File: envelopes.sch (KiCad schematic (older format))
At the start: 96 parts

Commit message: ENV1 inverter circuitry captured and simulated.
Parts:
- removed R? (x4): 100K, MyModules:SM0603-R-JRL, symbol R_US
- removed R? (x4): 10K, MyModules:SM0603-R-JRL, symbol R_US
- removed TP? (x4): TEST_POINT, MyModules:TEST_POINT_5000_SERIES, symbol TEST_POINT
- removed U?: TL074-, Housings_SSOP:TSSOP-14_4.4x5mm_Pitch0.65mm, symbol TL074-
- added Q?: MMBT3904, SOT-23, symbol MMBT3904
- added R? (x3): 100K, MyModules:SM0603-R-JRL, symbol R_US
- added R?: 10K, MyModules:SM0603-R-JRL, symbol R_US
- added R?: 47K, MyModules:SM0603-R-JRL, symbol R_US
- added U?: TL074-, Housings_SSOP:TSSOP-14_4.4x5mm_Pitch0.65mm, symbol TL074-
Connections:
- net EG2_GATE is gone; now on net GATE: R?.1, R?.2
- net GND: now also Q?.2 (E)
- net EG1_ATTACK_CV renamed ENV1_A
- net EG1_DECAY_CV renamed ENV1_D
- net EG1_ENV_OUT: no longer names the net of C?.1, R?.2, U?.1, U?.6 (THR)
- net EG1_ENV_OUT: now also R?.1, R?.1
- net EG1_GATE renamed GATE
- removed net EG1_INV_OUT: U?.1
- net EG1_RELEASE_CV renamed ENV1_R
- net EG1_SUSTAIN_CV renamed ENV1_S
- net EG2_ATTACK_CV renamed ENV2_A
- net EG2_DECAY_CV renamed ENV2_D
- net EG2_ENV_OUT: no longer names the net of C?.1, R?.2, U?.1, U?.6 (THR)
- net EG2_ENV_OUT: now also U?.12 (+)
- net EG2_RELEASE_CV renamed ENV2_R
- net EG2_SUSTAIN_CV renamed ENV2_S
- new net: R?.2, U?.12 (+)
- new net: R?.1, R?.2, U?.13 (-)
- new net: Q?.1 (B), R?.1
- new net: Q?.3 (C), R?.1, R?.2
- new net ENV1_POL: R?.2
- new net ENV_1: R?.2, U?.14
- new net ENV_2: U?.13 (-), U?.14
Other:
- note added: "ENV1 inversion works\nin simulation"
- moved on the sheet: C?, Q?, Q?A, R?, TP?, U?, U?A

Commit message: put oscillators into subsheet. slogging through ENV1/ENV2 switching
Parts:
- removed TP? (x4): TEST_POINT, MyModules:TEST_POINT_5000_SERIES, symbol TEST_POINT
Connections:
- net GND: now also U?.5 (+); no longer U?.3 (+)
- net at C?.1, R?.2, U?.12 (+)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: now also U?.7; no longer U?.1
- net at R?.1, R?.2, TP?.1: now also U?.8; no longer U?.1
- net at R?.1, R?.2: now also U?.9 (-); no longer U?.2 (-)
- net at R?.1, R?.2: now also U?.10 (+); no longer U?.3 (+)
- net at C?.2, Q?.6, Q?.6: now also U?.6 (-); no longer U?.2 (-)
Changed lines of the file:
@@
 $Descr D 34000 22000
 encoding utf-8
-Sheet 2 2
+Sheet 2 3
 Title ""
 Date ""
@@
 P 4075 9975
 F 0 "#PWR?" H 4075 10075 30  0001 C CNN
-F 1 "+12V" H 4050 10250 60  0000 C CNN
+F 1 "+12V" H 4050 10150 60  0000 C CNN
 F 2 "~" H 4075 9975 60  0000 C CNN
 F 3 "~" H 4075 9975 60  0000 C CNN
@@
 $Comp
 L TL074- U?
-U 1 1 57F64195
+U 3 1 57F64195
 P 25200 13700
 F 0 "U?" H 25250 13900 60  0000 C CNN
@@
 F 2 "Housings_SSOP:TSSOP-14_4.4x5mm_Pitch0.65mm" H 25200 13700 60  0001 C CNN
 F 3 "" H 25200 13700 60  0000 C CNN
-	1    25200 13700
+	3    25200 13700
 	-1   0    0    -1
 $EndComp
@@
 $Comp
 L TL074- U?
-U 1 1 57F641D3
+U 2 1 57F641D3
 P 26100 11125
 F 0 "U?" H 26150 11325 60  0000 C CNN
@@
 F 2 "Housings_SSOP:TSSOP-14_4.4x5mm_Pitch0.65mm" H 26100 11125 60  0001 C CNN
 F 3 "" H 26100 11125 60  0000 C CNN
-	1    26100 11125
+	2    26100 11125
 	1    0    0    -1
 $EndComp
@@
 P 19200 9975
 F 0 "#PWR?" H 19200 10075 30  0001 C CNN
-F 1 "+12V" H 19175 10250 60  0000 C CNN
+F 1 "+12V" H 19175 10150 60  0000 C CNN
 F 2 "~" H 19200 9975 60  0000 C CNN
 F 3 "~" H 19200 9975 60  0000 C CNN
@@
 $EndComp
 $Comp
-L TEST_POINT TP?
-U 1 1 57F64304
-P 21000 10725
-F 0 "TP?" V 21150 10675 60  0000 L CNN
-F 1 "TEST_POINT" H 21000 10780 30  0001 C CNN
-F 2 "MyModules:TEST_POINT_5000_SERIES" H 21000 10725 60  0001 C CNN
-F 3 "" H 21000 10725 60  0000 C CNN
-	1    21000 10725
-	0    -1   -1   0
-$EndComp
-$Comp
-L TEST_POINT TP?
-U 1 1 57F6430B
-P 20475 10725
-F 0 "TP?" V 20625 10675 60  0000 L CNN
-F 1 "TEST_POINT" H 20475 10780 30  0001 C CNN
-F 2 "MyModules:TEST_POINT_5000_SERIES" H 20475 10725 60  0001 C CNN
-F 3 "" H 20475 10725 60  0000 C CNN
-	1    20475 10725
-	0    -1   -1   0
-$EndComp
-$Comp
 L R_US R?
 U 1 1 57F64312
@@
 F 3 "" H 20700 10975 60  0000 C CNN
 	1    20700 10975
-	0    -1   -1   0
-$EndComp
-$Comp
-L TEST_POINT TP?
-U 1 1 57F64319
-P 20925 12125
-F 0 "TP?" V 20925 11900 60  0000 L CNN
-F 1 "TEST_POINT" H 20925 12180 30  0001 C CNN
-F 2 "MyModules:TEST_POINT_5000_SERIES" H 20925 12125 60  0001 C CNN
-F 3 "" H 20925 12125 60  0000 C CNN
-	1    20925 12125
-	0    -1   -1   0
-$EndComp
-$Comp
-L TEST_POINT TP?
-U 1 1 57F64320
-P 20400 12125
-F 0 "TP?" V 20400 12225 60  0000 L CNN
-F 1 "TEST_POINT" H 20400 12180 30  0001 C CNN
-F 2 "MyModules:TEST_POINT_5000_SERIES" H 20400 12125 60  0001 C CNN
-F 3 "" H 20400 12125 60  0000 C CNN
-	1    20400 12125
 	0    -1   -1   0
 $EndComp
@@
 	20900 10975 22650 10975
 Wire Wire Line
-	21000 10875 21000 10975
-Connection ~ 21000 10975
-Wire Wire Line
 	20250 12375 20450 12375
 Connection ~ 22300 10975
@@
 Connection ~ 24700 9575
 Wire Wire Line
-	20475 10875 20475 10975
-Connection ~ 20475 10975
-Wire Wire Line
 	21050 12375 21050 12675
-Wire Wire Line
-	20925 12275 20925 12375
-Wire Wire Line
-	20400 12275 20400 12375
-Connection ~ 20925 12375
-Connection ~ 20400 12375
 Connection ~ 24325 13700
 Wire Wire Line
@@
 U 1 1 57F684B3
 P 3475 9525
-F 0 "Q?" H 3675 9600 50  0000 L CNN
-F 1 "MMBT3904" H 3675 9525 50  0000 L CNN
-F 2 "SOT-23" H 3675 9450 50  0000 L CIN
+F 0 "Q?" H 3375 9825 50  0000 L CNN
+F 1 "MMBT3904" H 3100 9750 50  0000 L CNN
+F 2 "SOT-23" H 3675 9450 50  0001 L CIN
 F 3 "" H 3475 9525 50  0000 L CNN
 	1    3475 9525
@@
 U 1 1 57F68A9B
 P 18600 9525
-F 0 "Q?" H 18800 9600 50  0000 L CNN
-F 1 "MMBT3904" H 18800 9525 50  0000 L CNN
-F 2 "SOT-23" H 18800 9450 50  0000 L CIN
+F 0 "Q?" H 18500 9850 50  0000 L CNN
+F 1 "MMBT3904" H 18275 9750 50  0000 L CNN
+F 2 "SOT-23" H 18800 9450 50  0001 L CIN
 F 3 "" H 18600 9525 50  0000 L CNN
 	1    18600 9525

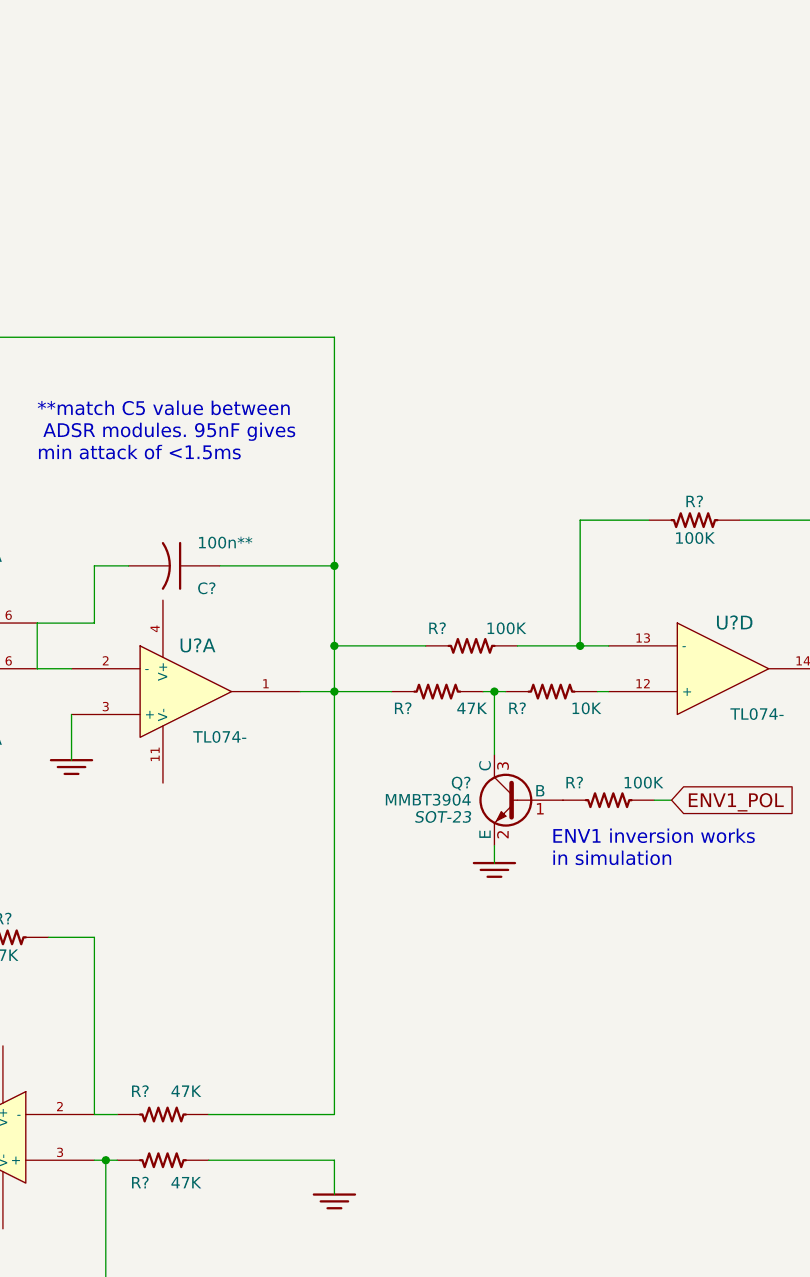
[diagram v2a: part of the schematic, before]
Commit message: working on a cross talk reduction circuit for CD4053. Seems pointless as it only works with unipolar signals. Try again another day stupid
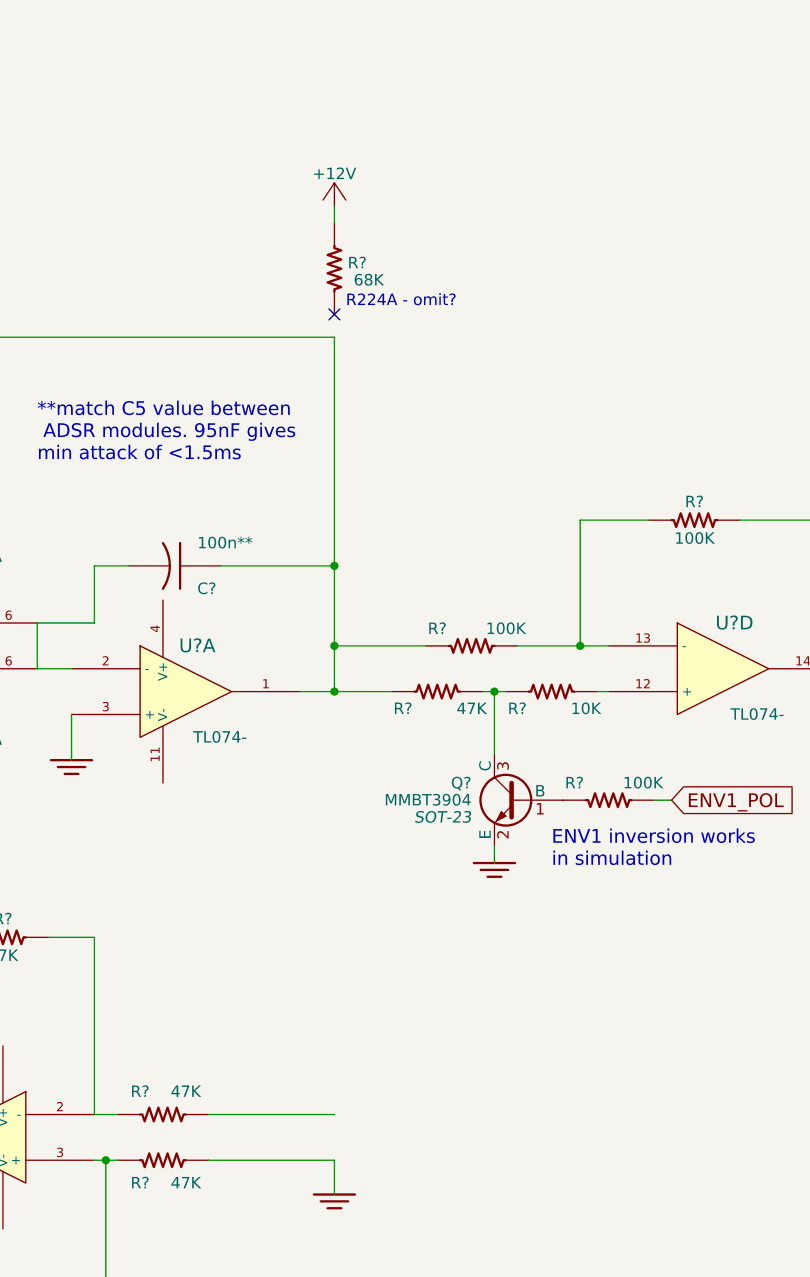
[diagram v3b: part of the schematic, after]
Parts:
- added R?: 68K, MyModules:SM0603-R-JRL, symbol R_US
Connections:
- net +12V: now also R?.2
- net at C?.1, R?.1, R?.1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: no longer R?.2
- no-connect marks 2 -> 3
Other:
- note added: "R224A - omit?"
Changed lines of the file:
@@
 	6325 9575 11625 9575
-Wire Wire Line
-	11625 9575 11625 12975
 Wire Wire Line
 	5925 12375 5925 12675
@@
 Text Notes 12575 11900 0    60   ~ 0
 ENV1 inversion works\nin simulation
+$Comp
+L R_US R?
+U 1 1 57FCB1DF
+P 11625 9275
+F 0 "R?" H 11525 9250 50  0000 C CNN
+F 1 "68K" H 11475 9325 50  0000 C CNN
+F 2 "MyModules:SM0603-R-JRL" H 11625 9275 60  0001 C CNN
+F 3 "" H 11625 9275 60  0001 C CNN
+F 4 "P10.0KCCT-ND" V 11625 9275 60  0001 C CNN "Digikey"
+	1    11625 9275
+	-1   0    0    1
+$EndComp
+$Comp
+L +12V #PWR?
+U 1 1 57FCB1E6
+P 11625 9000
+F 0 "#PWR?" H 11625 8850 50  0001 C CNN
+F 1 "+12V" H 11625 9140 50  0000 C CNN
+F 2 "" H 11625 9000 60  0000 C CNN
+F 3 "" H 11625 9000 60  0000 C CNN
+	1    11625 9000
+	-1   0    0    -1
+$EndComp
+Wire Wire Line
+	11625 9000 11625 9075
+Wire Wire Line
+	11625 9575 11625 11125
+NoConn ~ 11625 9475
+Text Notes 11675 9450 0    50   ~ 0
+R224A - omit?
 $EndSCHEMATC

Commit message: module board schematic basically captured. Need to doublecheck and confirm and try to simulation of VCA and VCF control
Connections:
- net at R?.2: now also C?.1, R?.1, R?.1, U?.1, U?.6 (THR)
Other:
- note added: "ENV 1"
- note added: "ENV 2"
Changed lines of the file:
@@
 Connection ~ 9425 10825
-Wire Wire Line
-	10325 10825 10325 11025
 Wire Wire Line
 	8525 10825 8525 11025
@@
 Connection ~ 24550 10825
 Wire Wire Line
-	25450 10825 25450 11025
-Wire Wire Line
 	23650 10825 23650 11025
 Wire Wire Line
@@
 F 0 "Q?" H 12625 11675 50  0000 L CNN
 F 1 "MMBT3904" H 12625 11600 50  0000 L CNN
-F 2 "SOT-23" H 12625 11525 50  0000 L CIN
+F 2 "SOT-23" H 12625 11525 50  0001 L CIN
 F 3 "" H 12425 11600 50  0000 L CNN
 	1    12425 11600
@@
 	11625 9000 11625 9075
 Wire Wire Line
-	11625 9575 11625 11125
+	11625 9575 11625 12975
 NoConn ~ 11625 9475
 Text Notes 11675 9450 0    50   ~ 0
 R224A - omit?
+Text Notes 3575 8350 0    200  ~ 40
+ENV 1
+Text Notes 18650 8350 0    200  ~ 40
+ENV 2
+Wire Wire Line
+	10400 10825 10400 11025
+Connection ~ 10400 11025
+Connection ~ 10400 10825
+Wire Wire Line
+	25525 10825 25525 11025
+Connection ~ 25525 11025
+Connection ~ 25525 10825
 $EndSCHEMATC

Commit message: sorting out packages, also taking deeper look at saw to tri converter. there are problems on 12V power and 10V saw that need to be sorted. NPN in tri converter is a an ultra fast switcher that might be hard to find an equiavalent for. Worth looking at tri waveform out of converter on JP8
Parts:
- gave numbers to parts that had none: 6
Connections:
- net ENV_1: now also U25.8; no longer U25.14
- net GND: now also U25.5 (+); no longer U25.3 (+)
- net at R?.2: now also U25.10 (+); no longer U25.12 (+)
- net at R?.1, R?.2: now also U25.9 (-); no longer U25.13 (-)
- net at R?.1, R?.2, TP?.1: now also U25.14; no longer U25.1
- net at R?.1, R?.2: now also U25.13 (-); no longer U25.2 (-)
- net at R?.1, R?.2: now also U25.12 (+); no longer U25.3 (+)
- net at C?.1, R?.1, R?.1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: now also U25.7; no longer U25.1
- net at C?.2, Q?.6, Q?.6: now also U25.6 (-); no longer U25.2 (-)
- net at R?.1, R?.2: now also U28.5 (+); no longer U28.10 (+)
- net at R?.1, R?.2, TP?.1: now also U28.7; no longer U28.8
- net at R?.1, R?.2: now also U28.6 (-); no longer U28.9 (-)

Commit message: more transistor swapping
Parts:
- removed Q? (x3): MMBT3904, SOT-23, symbol MMBT3904
- removed TP? (x4): TEST_POINT, MyModules:TEST_POINT_5000_SERIES, symbol TEST_POINT
- added Q? (x3): 2SC4738, SOT-23, symbol 2SC4738
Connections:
- net GND: now also Q?.2 (E), Q?.2 (E), Q?.2 (E)
- net at R?.1: now also Q?.1 (B)
- net at R?.1, R?.2: now also Q?.3 (C)
- net at C?.1, R?.1, U26.10 (A): now also Q?.3 (C)
- net at R?.1, R?.1: now also Q?.1 (B) (x2)
- net at C?.1, R?.1, U29.10 (A): now also Q?.3 (C)
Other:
- note added: "Change to PMP4201/5201 pairs?"
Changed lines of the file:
@@
-	0    -1   -1   0
-$EndComp
-$Comp
-L TEST_POINT TP?
-U 1 1 57F5ECCA
-P 9200 13525
-F 0 "TP?" V 9350 13475 60  0000 L CNN
-F 1 "TEST_POINT" H 9200 13580 30  0001 C CNN
-F 2 "MyModules:TEST_POINT_5000_SERIES" H 9200 13525 60  0001 C CNN
-F 3 "" H 9200 13525 60  0000 C CNN
-	1    9200 13525
-	0    -1   -1   0
-$EndComp
-$Comp
-L TEST_POINT TP?
-U 1 1 57F5ECD1
-P 8675 13525
-F 0 "TP?" V 8825 13475 60  0000 L CNN
-F 1 "TEST_POINT" H 8675 13580 30  0001 C CNN
-F 2 "MyModules:TEST_POINT_5000_SERIES" H 8675 13525 60  0001 C CNN
-F 3 "" H 8675 13525 60  0000 C CNN
-	1    8675 13525
 	0    -1   -1   0
 $EndComp
@@
 Wire Wire Line
 	5925 12375 5925 12675
-Connection ~ 9200 13675
 Wire Wire Line
 	4075 9975 4075 10150
 Wire Wire Line
 	4075 10150 4425 10150
-Connection ~ 8675 13675
 Connection ~ 9575 13075
 $Comp
@@
 $EndComp
 $Comp
-L TEST_POINT TP?
-U 1 1 57F6432E
-P 24325 13550
-F 0 "TP?" V 24475 13500 60  0000 L CNN
-F 1 "TEST_POINT" H 24325 13605 30  0001 C CNN
-F 2 "MyModules:TEST_POINT_5000_SERIES" H 24325 13550 60  0001 C CNN
-F 3 "" H 24325 13550 60  0000 C CNN
-	1    24325 13550
-	0    -1   -1   0
-$EndComp
-$Comp
-L TEST_POINT TP?
-U 1 1 57F64335
-P 23800 13550
-F 0 "TP?" V 23950 13500 60  0000 L CNN
-F 1 "TEST_POINT" H 23800 13605 30  0001 C CNN
-F 2 "MyModules:TEST_POINT_5000_SERIES" H 23800 13550 60  0001 C CNN
-F 3 "" H 23800 13550 60  0000 C CNN
-	1    23800 13550
-	0    -1   -1   0
-$EndComp
-$Comp
 L DMMT3906 Q?
 U 1 1 57F6433C
@@
 Wire Wire Line
 	26750 9575 26750 13600
-Connection ~ 24700 9575
 Wire Wire Line
 	21050 12375 21050 12675
-Connection ~ 24325 13700
 Wire Wire Line
 	19200 9975 19200 10150
 Wire Wire Line
 	19200 10150 19550 10150
-Connection ~ 23800 13700
-$Comp
-L MMBT3904 Q?
-U 1 1 57F684B3
-P 3475 9525
-F 0 "Q?" H 3375 9825 50  0000 L CNN
-F 1 "MMBT3904" H 3100 9750 50  0000 L CNN
-F 2 "SOT-23" H 3675 9450 50  0001 L CIN
-F 3 "" H 3475 9525 50  0000 L CNN
-	1    3475 9525
-	1    0    0    -1
-$EndComp
-$Comp
-L MMBT3904 Q?
-U 1 1 57F68A9B
-P 18600 9525
-F 0 "Q?" H 18500 9850 50  0000 L CNN
-F 1 "MMBT3904" H 18275 9750 50  0000 L CNN
-F 2 "SOT-23" H 18800 9450 50  0001 L CIN
-F 3 "" H 18600 9525 50  0000 L CNN
-	1    18600 9525
-	1    0    0    -1
-$EndComp
 Wire Wire Line
 	27400 10925 27400 10300
@@
 	13825 11025 14025 11025
 Connection ~ 13900 11025
-$Comp
-L MMBT3904 Q?
-U 1 1 57F5CE68
-P 12425 11600
-F 0 "Q?" H 12625 11675 50  0000 L CNN
-F 1 "MMBT3904" H 12625 11600 50  0000 L CNN
-F 2 "SOT-23" H 12625 11525 50  0001 L CIN
-F 3 "" H 12425 11600 50  0000 L CNN
-	1    12425 11600
-	-1   0    0    -1
-$EndComp
 $Comp
 L R_US R?
@@
 	-1   0    0    1
 $EndComp
+$Comp
+L 2SC4738 Q?
+U 1 1 585D55EC
+P 12425 11600
+F 0 "Q?" H 12625 11675 50  0000 L CNN
+F 1 "2SC4738" H 12625 11600 50  0000 L CNN
+F 2 "SOT-23" H 12625 11525 50  0001 L CIN
+F 3 "" H 12425 11600 50  0000 L CNN
+	1    12425 11600
+	-1   0    0    -1
+$EndComp
+$Comp
+L 2SC4738 Q?
+U 1 1 585D6B40
+P 18600 9525
+F 0 "Q?" H 18250 9750 50  0000 L CNN
+F 1 "2SC4738" H 18250 9675 50  0000 L CNN
+F 2 "SOT-23" H 18800 9450 50  0001 L CIN
+F 3 "" H 18600 9525 50  0000 L CNN
+	1    18600 9525
+	1    0    0    -1
+$EndComp
+$Comp
+L 2SC4738 Q?
+U 1 1 585D819F
+P 3475 9525
+F 0 "Q?" H 3075 9750 50  0000 L CNN
+F 1 "2SC4738" H 3075 9675 50  0000 L CNN
+F 2 "SOT-23" H 3675 9450 50  0001 L CIN
+F 3 "" H 3475 9525 50  0000 L CNN
+	1    3475 9525
+	1    0    0    -1
+$EndComp
+Text Notes 8475 9925 0    60   ~ 0
+Change to PMP4201/5201 pairs?
+Text Notes 23500 9900 0    60   ~ 0
+Change to PMP4201/5201 pairs?
 $EndSCHEMATC

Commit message: changing transistor matched pairs
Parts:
- removed Q? (x4): DMMT3904, MyModules:SOT363-JRL, symbol DMMT3904
- removed Q? (x4): DMMT3906, MyModules:SOT363-JRL, symbol DMMT3906
- added Q? (x4): PMP4201G, TO_SOT_Packages_SMD:SOT-353_SC-70-5, symbol PMP4201G
- added Q? (x4): PMP5201G, TO_SOT_Packages_SMD:SOT-353_SC-70-5, symbol PMP5201G
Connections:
- net GND: now also Q?.1 (B), Q?.1 (B), Q?.3 (B), Q?.3 (B)
- net at C?.2, R?.1, U25.2 (-): now also Q?.5 (C), Q?.5 (C)
- net at R?.2: now also Q?.2 (E), Q?.2 (E), Q?.2 (E), Q?.2 (E) (x2)
- net at C?.2, U25.6 (-): now also Q?.4 (C), Q?.4 (C)
- net at R?.2, R?.2, R?.2: now also Q?.3 (B) (x2)
- net at R?.2, R?.2, R?.2: now also Q?.1 (B) (x2)
- net at C?.2, R?.1, U28.2 (-): now also Q?.5 (C), Q?.5 (C)
- net at C?.2, U28.6 (-): now also Q?.4 (C), Q?.4 (C)
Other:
- note added: "Change to generate 0-5V response"
- note removed: "Change to PMP4201/5201 pairs?"

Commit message: changing up NJFETS
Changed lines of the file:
@@
 L GND_E #PWR?
 U 1 1 57F5EAD9
-P 9125 11600
-F 0 "#PWR?" V 9125 11600 30  0001 C CNN
-F 1 "GND_E" H 9125 11530 30  0001 C CNN
-F 2 "~" H 9125 11600 60  0000 C CNN
-F 3 "~" H 9125 11600 60  0000 C CNN
-	1    9125 11600
+P 9125 11425
+F 0 "#PWR?" V 9125 11425 30  0001 C CNN
+F 1 "GND_E" H 9125 11355 30  0001 C CNN
+F 2 "~" H 9125 11425 60  0000 C CNN
+F 3 "~" H 9125 11425 60  0000 C CNN
+	1    9125 11425
 	1    0    0    -1
 $EndComp
@@
 L GND_E #PWR?
 U 1 1 57F5EADF
-P 9725 11600
-F 0 "#PWR?" V 9725 11600 30  0001 C CNN
-F 1 "GND_E" H 9725 11530 30  0001 C CNN
-F 2 "~" H 9725 11600 60  0000 C CNN
-F 3 "~" H 9725 11600 60  0000 C CNN
-	1    9725 11600
+P 9725 11425
+F 0 "#PWR?" V 9725 11425 30  0001 C CNN
+F 1 "GND_E" H 9725 11355 30  0001 C CNN
+F 2 "~" H 9725 11425 60  0000 C CNN
+F 3 "~" H 9725 11425 60  0000 C CNN
+	1    9725 11425
 	1    0    0    -1
 $EndComp
@@
 	6425 9775 6475 9775
 Wire Wire Line
-	6475 9775 6475 8575
-Wire Wire Line
-	6475 8575 5075 8575
-Wire Wire Line
-	5075 8575 4675 8575
-Wire Wire Line
-	4675 8575 4475 8575
-Wire Wire Line
-	4475 8575 3575 8575
+	6475 8575 6475 9775
+Wire Wire Line
+	3575 8575 4475 8575
+Wire Wire Line
+	4475 8575 4675 8575
+Wire Wire Line
+	4675 8575 5075 8575
+Wire Wire Line
+	5075 8575 6475 8575
 Wire Wire Line
 	3575 8575 3575 8625
@@
 	8525 10925 8525 11025
 Wire Wire Line
-	9125 11325 9125 11600
-Wire Wire Line
-	9725 11325 9725 11600
+	9125 11325 9125 11425
+Wire Wire Line
+	9725 11325 9725 11425
 Wire Wire Line
 	9925 10825 10400 10825
@@
 L GND_E #PWR?
 U 1 1 57F6414C
-P 24250 11625
-F 0 "#PWR?" V 24250 11625 30  0001 C CNN
-F 1 "GND_E" H 24250 11555 30  0001 C CNN
-F 2 "~" H 24250 11625 60  0000 C CNN
-F 3 "~" H 24250 11625 60  0000 C CNN
-	1    24250 11625
+P 24250 11425
+F 0 "#PWR?" V 24250 11425 30  0001 C CNN
+F 1 "GND_E" H 24250 11355 30  0001 C CNN
+F 2 "~" H 24250 11425 60  0000 C CNN
+F 3 "~" H 24250 11425 60  0000 C CNN
+	1    24250 11425
 	1    0    0    -1
 $EndComp
@@
 L GND_E #PWR?
 U 1 1 57F64152
-P 24850 11625
-F 0 "#PWR?" V 24850 11625 30  0001 C CNN
-F 1 "GND_E" H 24850 11555 30  0001 C CNN
-F 2 "~" H 24850 11625 60  0000 C CNN
-F 3 "~" H 24850 11625 60  0000 C CNN
-	1    24850 11625
+P 24850 11425
+F 0 "#PWR?" V 24850 11425 30  0001 C CNN
+F 1 "GND_E" H 24850 11355 30  0001 C CNN
+F 2 "~" H 24850 11425 60  0000 C CNN
+F 3 "~" H 24850 11425 60  0000 C CNN
+	1    24850 11425
 	1    0    0    -1
 $EndComp
@@
 	21550 9775 21600 9775
 Wire Wire Line
-	21600 9775 21600 8575
-Wire Wire Line
-	21600 8575 20200 8575
-Wire Wire Line
-	20200 8575 19800 8575
-Wire Wire Line
-	19800 8575 19600 8575
-Wire Wire Line
-	19600 8575 18700 8575
+	21600 8575 21600 9775
+Wire Wire Line
+	18700 8575 19600 8575
+Wire Wire Line
+	19600 8575 19800 8575
+Wire Wire Line
+	19800 8575 20200 8575
+Wire Wire Line
+	20200 8575 21600 8575
 Wire Wire Line
 	18700 8575 18700 8625
@@
 	23650 10925 23650 11025
 Wire Wire Line
-	24250 11325 24250 11625
-Wire Wire Line
-	24850 11325 24850 11625
+	24250 11325 24250 11425
+Wire Wire Line
+	24850 11325 24850 11425
 Wire Wire Line
 	25050 10825 25525 10825
